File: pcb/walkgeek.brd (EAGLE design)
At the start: 101.5 x 40 mm, 124 parts, among them M1 NOKIA1100_VIBRATOR, X1 NOKIA1100_EXT_CONN, X2 MICROSD_CONN

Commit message: Ported OPUS
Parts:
- C19, C20: value 0.1uF -> N/A
- R36: value 220K -> N/A
- R37: value 220K -> 0
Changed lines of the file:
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@@
 <element name="DD3" library="walkgeek-eagle" package="TSOT23-5" value="LTC4054ES5-4.2" x="88" y="9.5" rot="R90"/>
 <element name="R35" library="walkgeek-eagle" package="R0805" value="1.65K 1%" x="78.9" y="10.2" rot="R270"/>
-<element name="R36" library="walkgeek-eagle" package="R0805" value="220K" x="76.6" y="7.1" rot="R270"/>
-<element name="R37" library="walkgeek-eagle" package="R0805" value="220K" x="78.9" y="7.1" rot="R270"/>
-<element name="C19" library="walkgeek-eagle" package="C0805" value="0.1uF" x="74.3" y="7.1" rot="R90"/>
+<element name="R36" library="walkgeek-eagle" package="R0805" value="N/A" x="76.6" y="7.1" rot="R270"/>
+<element name="R37" library="walkgeek-eagle" package="R0805" value="0" x="78.9" y="7.1" rot="R270"/>
+<element name="C19" library="walkgeek-eagle" package="C0805" value="N/A" x="74.3" y="7.1" rot="R90"/>
 <element name="R38" library="walkgeek-eagle" package="R0805" value="220K" x="23.2" y="4.2" rot="R270"/>
 <element name="R39" library="walkgeek-eagle" package="R0805" value="220K" x="20.2" y="3.7"/>
-<element name="C20" library="walkgeek-eagle" package="C0805" value="0.1uF" x="25.4" y="4.2" rot="R90"/>
+<element name="C20" library="walkgeek-eagle" package="C0805" value="N/A" x="25.4" y="4.2" rot="R90"/>
 <element name="C21" library="walkgeek-eagle" package="C0805" value="1uF" x="86.9" y="14.7" rot="R180"/>
 <element name="R40" library="walkgeek-eagle" package="R1206" value="1.8" x="87.95" y="12.5" rot="R180"/>

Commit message: PowerManager fixes
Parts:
- removed C19, C20: N/A, walkgeek-eagle:C0805
- removed R36: N/A, walkgeek-eagle:R0805
- removed R37: 0, walkgeek-eagle:R0805
- R35: value 1.65K 1% -> 2K 1%
- R38, R39: value 220K -> 10K 1%
- moved R39 55.5 mm to (75.6, 6.50)
- moved R38 55.3 mm to (78.5, 6.00), turned to 90 degrees
- moved VT3 0.20 mm to (96.9, 10.5)
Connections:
- removed net N$15: DD3.5, R35.2, R37.1
- net ADC_BAT: no longer C20.1
- net ADC_CHG: now also DD3.5, R35.2; no longer C19.1, R36.2, R37.2
- net GND: no longer C19.2, C20.2, R36.1
- net N$17: now also R39.1
- net VBAT0: no longer R39.1
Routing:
- net ADC_BAT: track 95.4 -> 36.9 mm
- net N$17: track 8.60 -> 31.3 mm, vias 0 -> 2
- net N$15: track 13.3 -> 0.00 mm
- net VBAT0: track 140.7 -> 134.4 mm
- net ADC_CHG: track 40.4 -> 37.5 mm
- net GND: track 110.1 -> 109.4 mm

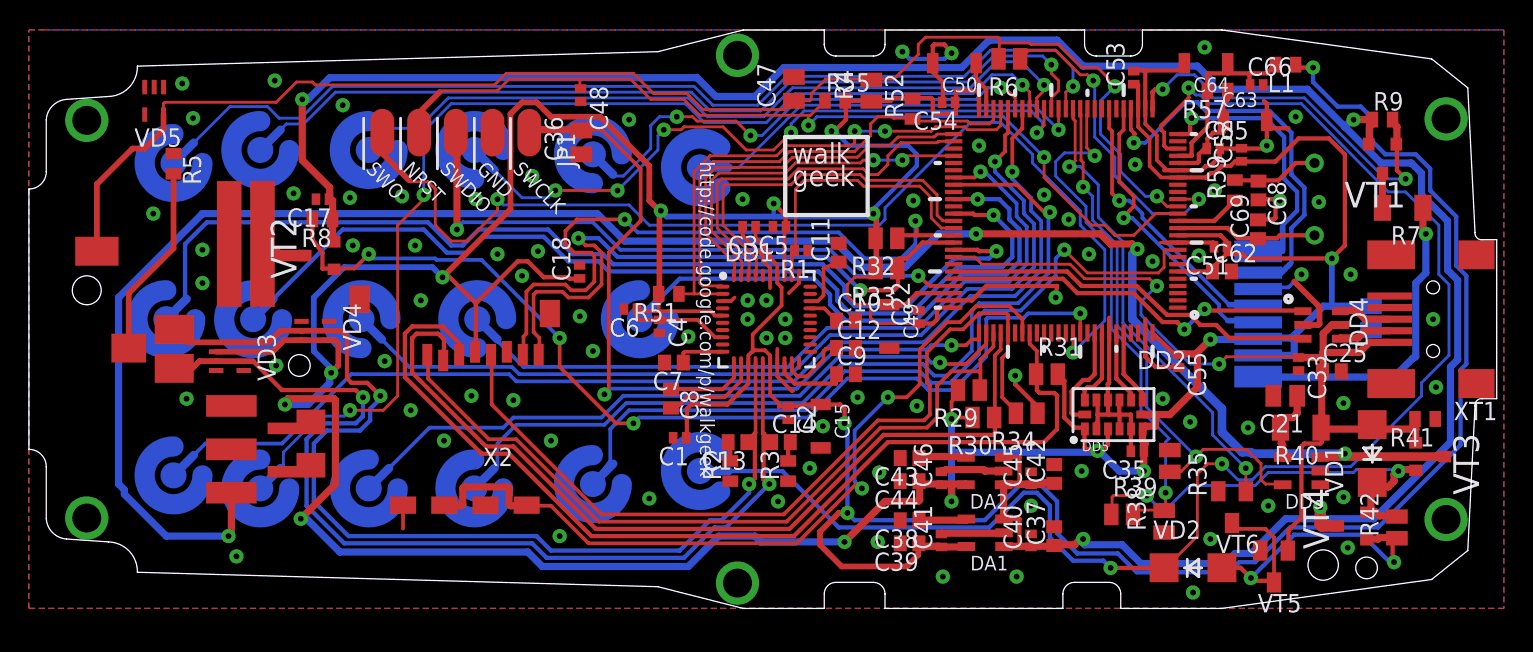
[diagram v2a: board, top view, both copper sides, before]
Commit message: Corrected pcb numbering and captions
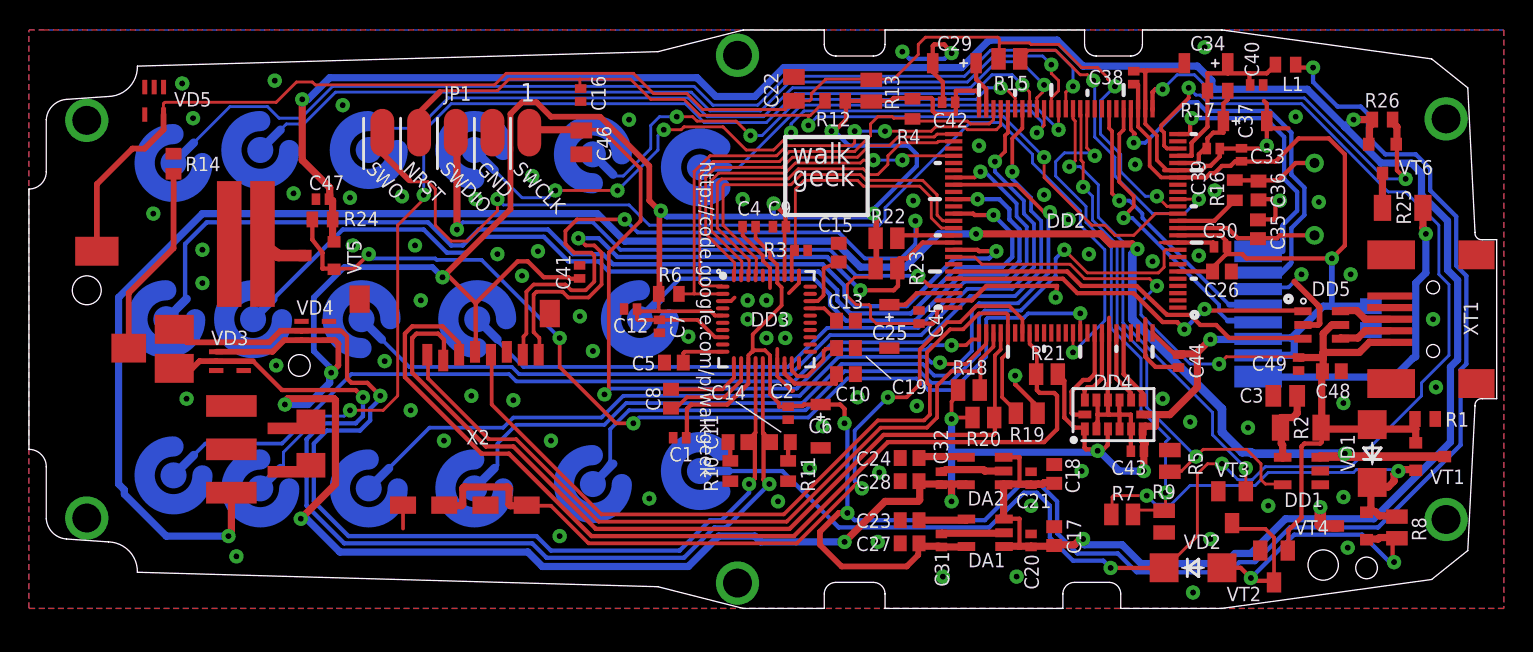
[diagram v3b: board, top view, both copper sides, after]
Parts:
- removed C52, C53, C54, C55, C65, C66: 0.1uF, walkgeek-eagle:C0402
- removed C63: 1uF, walkgeek-eagle:SMC_A
- removed C68, C69: 20pF, walkgeek-eagle:C0603
- removed R35: 2K 1%, walkgeek-eagle:R0805
- removed R38, R39: 10K 1%, walkgeek-eagle:R0805
- removed R40: 1.8, walkgeek-eagle:R1206
- removed R41: 10K, walkgeek-eagle:R0603
- removed R42: 10K, walkgeek-eagle:R0805
- removed R51, R52: 4.7K, walkgeek-eagle:R0603
- added C19, C27, C28: 1uF, walkgeek-eagle:C0603
- added C20, C31, C32: 0.1uF, walkgeek-eagle:C0402
- added C23, C24: 0.01uF, walkgeek-eagle:C0603
- added C29: 2.2uF, walkgeek-eagle:SMC_A
- added R10, R11: 51, walkgeek-eagle:R0603
- added R13: 10K, walkgeek-eagle:R0805
- added R14: 0, walkgeek-eagle:R0603
- added R15: 1K, walkgeek-eagle:R0805
- added R24, R26: 10K, walkgeek-eagle:R0603
- added R25: 33(*), walkgeek-eagle:R1206
- C10: value 150pF -> 1uF
- C11: value 150pF -> 0.022uF
- C12, C39, C42, C44, C7, C9: value 1uF -> 0.1uF; device walkgeek-eagle:C0603 -> walkgeek-eagle:C0402
- C13: value 0.022uF -> 150pF
- C15: value 1uF -> 150pF; device walkgeek-eagle:SMC_A -> walkgeek-eagle:C0603
- C16: device walkgeek-eagle:C0805 -> walkgeek-eagle:C0402
- C17, C18, C5: value 0.1uF -> 1uF; device walkgeek-eagle:C0402 -> walkgeek-eagle:C0603
- C21: value 1uF -> 0.1uF; device walkgeek-eagle:C0805 -> walkgeek-eagle:C0402
- C22: value 0.1uF -> 0.01uF; device walkgeek-eagle:C0402 -> walkgeek-eagle:C0805
- C25: value 0.01uF -> 2.2uF; device walkgeek-eagle:C0603 -> walkgeek-eagle:SMC_A
- C3: value 0.1uF -> 1uF; device walkgeek-eagle:C0402 -> walkgeek-eagle:C0805
- C35: value 0.1uF -> 20pF; device walkgeek-eagle:C0402 -> walkgeek-eagle:C0603
- C36: value 100pF -> 20pF; device walkgeek-eagle:C0805 -> walkgeek-eagle:C0603
- C37: device walkgeek-eagle:C0603 -> walkgeek-eagle:SMC_A
- C38, C43: value 0.01uF -> 0.1uF; device walkgeek-eagle:C0603 -> walkgeek-eagle:C0402
- C46: value 0.1uF -> 100pF; device walkgeek-eagle:C0402 -> walkgeek-eagle:C0805
- C47: value 0.01uF -> 0.1uF; device walkgeek-eagle:C0805 -> walkgeek-eagle:C0402
- C48: value 0.1uF -> 0.01uF; device walkgeek-eagle:C0402 -> walkgeek-eagle:C0603
- C49: value 2.2uF -> 0.1uF; device walkgeek-eagle:SMC_A -> walkgeek-eagle:C0402
- C50: value 2.2uF -> 0.1uF; device walkgeek-eagle:SMC_A -> walkgeek-eagle:C0805
- C6: value 0.1uF -> 1uF; device walkgeek-eagle:C0402 -> walkgeek-eagle:SMC_A
- DD1: value CS43L22 -> LTC4054ES5-4.2; device walkgeek-eagle:QFN40-6X6 -> walkgeek-eagle:TSOT23-5
- DD3: value LTC4054ES5-4.2 -> CS43L22; device walkgeek-eagle:TSOT23-5 -> walkgeek-eagle:QFN40-6X6
- DD4: value USBLC6-2SC6 -> LIS302DL; device walkgeek-eagle:SOT23-6L -> walkgeek-eagle:LGA14
- DD5: value LIS302DL -> USBLC6-2SC6; device walkgeek-eagle:LGA14 -> walkgeek-eagle:SOT23-6L
- R1: device walkgeek-eagle:R0402 -> walkgeek-eagle:R0603
- R2: value 51 -> 1.8; device walkgeek-eagle:R0603 -> walkgeek-eagle:R1206
- R3: value 51 -> 10K; device walkgeek-eagle:R0603 -> walkgeek-eagle:R0402
- R4: value 10K -> 4.7K; device walkgeek-eagle:R0805 -> walkgeek-eagle:R0603
- R5: value 0 -> 2K 1%; device walkgeek-eagle:R0603 -> walkgeek-eagle:R0805
- R6: value 1K -> 4.7K; device walkgeek-eagle:R0805 -> walkgeek-eagle:R0603
- R7: value 33(*) -> 10K 1%; device walkgeek-eagle:R1206 -> walkgeek-eagle:R0805
- R8: device walkgeek-eagle:R0603 -> walkgeek-eagle:R0805
- R9: value 10K -> 10K 1%; device walkgeek-eagle:R0603 -> walkgeek-eagle:R0805
- VT2, VT3: value IRLML6402 -> BCR135; device walkgeek-eagle:MICRO3 -> walkgeek-eagle:SOT23-BEC
- VT5, VT6: value BCR135 -> IRLML6402; device walkgeek-eagle:SOT23-BEC -> walkgeek-eagle:MICRO3
- moved R8 77.3 mm to (94.6, 5.60), turned to 90 degrees
- moved R5 71.9 mm to (78.9, 10.2)
- moved VT2 69.4 mm to (86.1, 2.90), turned to 180 degrees
- moved VT5 69.4 mm to (20.1, 24.4), turned to 90 degrees
- moved C16 56.8 mm to (38.1, 35.5), flipped to the top
- moved C17 55.7 mm to (70.9, 5.00), turned to 90 degrees
- moved C48 55.3 mm to (90.1, 16.4), turned to 0 degrees
- moved C36 46.9 mm to (85.0, 28.9), turned to 270 degrees
- moved R1 44.7 mm to (96.5, 13.1)
- moved R2 39.6 mm to (88.0, 12.5), turned to 180 degrees
- moved C3 38.9 mm to (86.9, 14.7)
- moved DD1 38.5 mm to (88.0, 9.50), turned to 90 degrees
- moved DD3 38.5 mm to (51.0, 20.0), turned to 0 degrees
- moved SB12 37.6 mm to (46.4, 30.5), turned to 315 degrees
- moved C18 35.7 mm to (70.9, 9.30)
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- renumbered C51 to C30, C62 to C26, C64 to C34, R29 to R18, R30 to R20, R31 to R21, R32 to R22, R33 to R23, R34 to R19, R55 to R12, R57 to R17, R59 to R16, ZQ2 to ZQ1
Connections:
- net #PRST: now also DD3.32, R3.2; no longer DD1.32, R1.2
- net +2V5: now also C27.1, C31.1, C4.1, C6.+, DD3.13, DD3.16, DD3.34; no longer C15.+, C3.1, C39.1, C41.1, DD1.13, DD1.16, DD1.34
- net +3V3: now also C12.1, C28.1, C32.1, C33.1, C38.1, C41.1, C42.1, C43.1, C45.1, C50.1, C7.1, C9.1, DD3.33, DD3.5, DD3.8, DD4.1, DD4.3, DD4.6, DD4.7, R13.1, R4.2, R6.2; no longer C16.1, C18.1, C22.1, C35.1, C4.1, C46.1, C5.1, C52.1, C53.1, C54.1, C55.1, C6.1, DD1.33, DD1.5, DD1.8, DD5.1, DD5.3, DD5.6, DD5.7, R4.1, R51.2, R52.2
- net ADC_BAT: now also R7.2, R9.2; no longer R38.2, R39.2
- net ADC_CHG: now also DD1.5, R5.2; no longer DD3.5, R35.2
- net BTN_ADC: now also C22.1, R13.2, R15.2; no longer C47.1, R4.2, R6.2
- net BTN_OUT: now also R15.1; no longer R6.1
- net B_0: now also SB11.INNER; no longer SB16.INNER
- net B_1: now also SB3.INNER; no longer SB6.INNER
- net B_2: now also SB8.INNER; no longer SB7.INNER
- net B_3: now also SB14.INNER; no longer SB8.INNER
- net B_4: now also SB4.INNER; no longer SB9.INNER
- net B_5: now also SB9.INNER; no longer SB10.INNER
- net B_6: now also SB15.INNER; no longer SB11.INNER
- net B_7: now also SB5.INNER; no longer SB12.INNER
- net B_8: now also SB10.INNER; no longer SB13.INNER
- net B_9: now also SB16.INNER; no longer SB14.INNER
- net B_AST: now also SB6.INNER; no longer SB15.INNER
- net B_DWN: now also SB13.INNER; no longer SB5.INNER
- net B_SEL: now also SB7.INNER; no longer SB4.INNER
- net B_UP: now also SB12.INNER; no longer SB3.INNER
- net D_NBKL: now also R26.2, VT6.1; no longer R9.2, VT1.1
- net GND: now also C13.2, C15.2, C19.2, C20.2, C23.2, C24.2, C25.-, C27.2, C28.2, C29.-, C31.2, C32.2, C36.2, C37.-, C46.1, C49.2, C50.2, C6.-, DD1.2, DD3.17, DD3.3, DD3.31, DD3.35, DD3.EXP@3, DD3.EXP@4, DD3.EXP@5, DD3.EXP@9, DD4.10, DD4.11, DD4.12, DD4.4, DD4.5, R10.1, R11.1, R14.1, R9.1, VT2.E, VT3.E; no longer C11.2, C15.-, C25.2, C36.1, C37.2, C46.2, C49.-, C50.-, C52.2, C53.2, C54.2, C55.2, C6.2, C63.-, C65.2, C66.2, C68.2, C69.2, DD1.17, DD1.3, DD1.31, DD1.35, DD1.EXP@3, DD1.EXP@4, DD1.EXP@5, DD1.EXP@9, DD3.2, DD5.10, DD5.11, DD5.12, DD5.4, DD5.5, R2.1, R35.1, R38.1, R41.1, VT5.E, VT6.E
- net I2S_MCK: now also DD3.37; no longer DD1.37
- net I2S_SCK: now also DD3.38; no longer DD1.38
- net I2S_SD: now also DD3.39; no longer DD1.39
- net I2S_WS: now also DD3.40; no longer DD1.40
- net MEMS_INT1: now also DD4.8; no longer DD5.8
- net MEMS_INT2: now also DD4.9; no longer DD5.9
- net MEMS_SCL: now also DD4.14; no longer DD5.14
- net MEMS_SDA: now also DD4.13; no longer DD5.13
- net N$1: now also R25.1; no longer R7.1
- net N$10: now also C5.1, DD3.10; no longer C7.1, DD1.10
- net N$11: now also R14.2; no longer R5.2
- net N$12: now also C11.2, R10.2; no longer C13.2, R2.2
- net N$13: now also R11.2; no longer R3.2
- net N$14: now also VT5.3; no longer VT2.3
- net N$16: now also C3.1, DD1.4, R2.2; no longer C21.1, DD3.4, R40.2
- net N$17: now also R7.1, R8.2, VT1.2; no longer R39.1, R42.2, VT3.2
- net N$19: now also R25.2, VT6.3; no longer R7.2, VT1.3
- net N$2: now also C10.1, DD3.18; no longer C9.1, DD1.18
- net N$21: now also R8.1, VT2.C, VT3.C; no longer R42.1, VT5.C, VT6.C
- net N$22: now also DD5.6; no longer DD4.6
- net N$29: now also DD5.4; no longer DD4.4
- net N$3: now also C13.1, DD3.27; no longer C10.1, DD1.27
- net N$31: now also C25.+; no longer C49.+
- net N$33: now also C35.1; no longer C69.1
- net N$34: now also C24.1; no longer C43.1
- net N$35: now also C23.1; no longer C38.1
- net N$38: now also C29.+; no longer C50.+
- net N$4: now also C15.1, DD3.28; no longer C11.1, DD1.28
- net N$40: now also C40.1; no longer C66.1
- net N$42: now also C37.+, C39.1; no longer C63.+, C65.1
- net N$44: now also C36.1; no longer C68.1
- net N$5: now also C19.1, DD3.19; no longer C12.1, DD1.19
- net N$6: now also C11.1, DD3.14; no longer C13.1, DD1.14
- net N$7: now also DD3.15; no longer DD1.15
- net N$8: now also DD3.11; no longer DD1.11
- net N$9: now also DD3.12; no longer DD1.12
- net NRST: now also C16.1; no longer C48.1
- net NVBTR: now also R24.2, VT5.1; no longer R8.2, VT2.1
- net PWR_EN: now also VT3.B; no longer VT6.B
- net SCL: now also DD3.2, R6.1; no longer DD1.2, R51.1
- net SDA: now also DD3.1, R4.1; no longer DD1.1, R52.1
- net SWCLK: now also C46.2; no longer C36.2
- net U_DM: now also DD5.3; no longer DD4.3
- net U_DP: now also DD5.1; no longer DD4.1
- net VBAT: now also C18.1, C20.1, C21.1, C47.1, R24.1, R26.1, VT5.2, VT6.2; no longer C37.1, C40.1, C42.1, C45.1, R8.1, R9.1, VT1.2, VT2.2
- net VBAT0: now also DD1.3, VT1.3; no longer DD3.3, VT3.3
- net VBUS: now also C48.1, C49.1, DD5.5, R1.2, R2.1, VT1.1, VT2.B; no longer C25.1, C33.1, DD4.5, R40.1, R41.2, VT3.1, VT5.B
